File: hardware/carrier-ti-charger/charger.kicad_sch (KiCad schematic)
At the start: 42 parts, among them J2 NTC, Q10 2N7002, Q12 2N7002, Q13 CSD17575Q3, SW4 RESET 6x6, U14 TPS259474LRPWR, U4 BQ25798RQMR

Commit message: Refine resistors.
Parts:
- L1: value 2.2uH FXL0630-2R2-M -> 2.2uH FC-ALX4030D-2R2MT; footprint carrier:IND-SMD_L7.0-W6.6_FXL0630 -> carrier:IND-SMD_L4.2-W4.2_FC-ALX4030D; LCSC C167218 -> C5370906
- R77: footprint carrier:R_0805_2012Metric_NoSilk -> Resistor_SMD:R_0603_1608Metric; LCSC C706247 -> C2924137; MPN RT0805BRD075K36L -> AR03BTCX5361A; Manufacturer YAGEO -> Viking Tech
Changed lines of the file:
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@@
 			)
 		)
-		(property "Value" "2.2uH FXL0630-2R2-M"
+		(property "Value" "2.2uH FC-ALX4030D-2R2MT"
 			(at 139.7 69.85 0)
 			(show_name no)
@@
 			)
 		)
-		(property "Footprint" "carrier:IND-SMD_L7.0-W6.6_FXL0630"
+		(property "Footprint" "carrier:IND-SMD_L4.2-W4.2_FC-ALX4030D"
 			(at 139.7 64.77 0)
 			(hide yes)
@@
 			)
 		)
-		(property "Datasheet" "https://datasheet.lcsc.com/datasheet/pdf/7ccab6d15d9e909aa3f3d55ed931dfcf.pdf?productCode=C167216"
+		(property "Datasheet" "https://datasheet.lcsc.com/datasheet/pdf/4f0a80287f31a1fb9e399a39619e691e.pdf?productCode=C5370906"
 			(at 139.7 64.77 0)
 			(hide yes)
@@
 			)
 		)
-		(property "LCSC" "C167218"
+		(property "LCSC" "C5370906"
 			(at 139.7 64.77 0)
 			(hide yes)
@@
 			)
 		)
-		(property "Footprint" "carrier:R_0805_2012Metric_NoSilk"
+		(property "Footprint" "Resistor_SMD:R_0603_1608Metric"
 			(at 215.9 57.15 0)
 			(hide yes)
@@
 			)
 		)
-		(property "Datasheet" "https://datasheet.lcsc.com/datasheet/pdf/46d7760c582640714d605308a25a220a.pdf?productCode=C706247"
+		(property "Datasheet" "https://datasheet.lcsc.com/datasheet/pdf/5bf30c62a4b85499d309118a7d825f44.pdf?productCode=C2924137"
 			(at 215.9 57.15 0)
 			(hide yes)
@@
 			)
 		)
-		(property "Description" "OVLO divider, 0.1%, 25 ppm/C, 125 mW, 150 V"
+		(property "Description" "OVLO divider, 0.1%, 25 ppm/C, 100 mW, 75 V"
 			(at 215.9 57.15 0)
 			(hide yes)
@@
 			)
 		)
-		(property "LCSC" "C706247"
+		(property "LCSC" "C2924137"
 			(at 215.9 57.15 0)
 			(hide yes)
@@
 			)
 		)
-		(property "MPN" "RT0805BRD075K36L"
+		(property "MPN" "AR03BTCX5361A"
 			(at 215.9 57.15 0)
 			(hide yes)
@@
 			)
 		)
-		(property "Manufacturer" "YAGEO"
+		(property "Manufacturer" "Viking Tech"
 			(at 215.9 57.15 0)
 			(hide yes)

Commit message: Fix missing parts.
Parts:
- D10: value BAT54WS -> 1N4148WS; LCSC C22629 -> C2128; MPN (none) -> 1N4148WS
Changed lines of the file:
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@@
 			)
 		)
-		(property "Value" "BAT54WS"
+		(property "Value" "1N4148WS"
 			(at 38.1 92.71 0)
 			(show_name no)
@@
 			)
 		)
-		(property "LCSC" "C22629"
+		(property "LCSC" "C2128"
 			(at 38.1 90.17 0)
 			(hide yes)
+			(show_name no)
+			(do_not_autoplace no)
+			(effects
+				(font
+					(size 1.27 1.27)
+				)
+			)
+		)
+		(property "MPN" "1N4148WS"
+			(at 38.1 90.17 0)
+			(hide yes)

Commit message: Consolidate bom.
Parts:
- C33: value 22u 16V X7R -> 22u 10V X7R; footprint Capacitor_SMD:C_1206_3216Metric -> Capacitor_SMD:C_0805_2012Metric; LCSC C385906 -> C907991
- C43, C44, C46, C5, C50: value 100n 50V -> 100n 16V; footprint Capacitor_SMD:C_0603_1608Metric -> carrier:C_0402_1005Metric_NoSilk; LCSC C14663 -> C1525; MPN (none) -> CL05B104KO5NNNC
- R56: footprint Resistor_SMD:R_0603_1608Metric -> carrier:R_0402_1005Metric_NoSilk; LCSC C23162 -> C25900; MPN (none) -> 0402WGF4701TCE
- R60: footprint Resistor_SMD:R_0603_1608Metric -> carrier:R_0402_1005Metric_NoSilk; LCSC C2933258 -> C49196905; MPN (none) -> FRC0402F7683TS
- R77: value 5.36k -> 4.7k 1%; footprint Resistor_SMD:R_0603_1608Metric -> carrier:R_0402_1005Metric_NoSilk; LCSC C2924137 -> C25900; MPN AR03BTCX5361A -> 0402WGF4701TCE; TCR 25 ppm/C -> 100 ppm/C; Tolerance 0.1% -> 1%
- R78: value 1.5k -> 1.24k 0.1%; LCSC C281775 -> C2984409; MPN RT0402BRD071K5L -> ARG02BTC1241
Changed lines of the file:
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@@
 			)
 		)
-		(property "Value" "100n 50V"
+		(property "Value" "100n 16V"
 			(at 182.88 52.07 0)
 			(show_name no)
@@
 			)
 		)
-		(property "Footprint" "Capacitor_SMD:C_0603_1608Metric"
+		(property "Footprint" "carrier:C_0402_1005Metric_NoSilk"
 			(at 180.34 50.8 0)
 			(hide yes)
@@
 			)
 		)
-		(property "LCSC" "C14663"
+		(property "LCSC" "C1525"
+			(at 180.34 50.8 0)
+			(hide yes)
+			(show_name no)
+			(do_not_autoplace no)
+			(effects
+				(font
+					(size 1.27 1.27)
+				)
+			)
+		)
+		(property "MPN" "CL05B104KO5NNNC"
 			(at 180.34 50.8 0)
 			(hide yes)
@@
 			)
 		)
-		(property "Value" "100n 50V"
+		(property "Value" "100n 16V"
 			(at 194.31 140.97 0)
 			(show_name no)
@@
 			)
 		)
-		(property "Footprint" "Capacitor_SMD:C_0603_1608Metric"
+		(property "Footprint" "carrier:C_0402_1005Metric_NoSilk"
 			(at 191.77 139.7 0)
 			(hide yes)
@@
 			)
 		)
-		(property "LCSC" "C14663"
+		(property "LCSC" "C1525"
+			(at 191.77 139.7 0)
+			(hide yes)
+			(show_name no)
+			(do_not_autoplace no)
+			(effects
+				(font
+					(size 1.27 1.27)
+				)
+			)
+		)
+		(property "MPN" "CL05B104KO5NNNC"
 			(at 191.77 139.7 0)
 			(hide yes)
@@
 			)
 		)
-		(property "Value" "100n 50V"
+		(property "Value" "100n 16V"
 			(at 31.75 59.69 0)
 			(show_name no)
@@
 			)
 		)
-		(property "Footprint" "Capacitor_SMD:C_0603_1608Metric"
+		(property "Footprint" "carrier:C_0402_1005Metric_NoSilk"
 			(at 29.21 58.42 0)
 			(hide yes)
@@
 			)
 		)
-		(property "LCSC" "C14663"
+		(property "LCSC" "C1525"
+			(at 29.21 58.42 0)
+			(hide yes)
+			(show_name no)
+			(do_not_autoplace no)
+			(effects
+				(font
+					(size 1.27 1.27)
+				)
+			)
+		)
+		(property "MPN" "CL05B104KO5NNNC"
 			(at 29.21 58.42 0)
 			(hide yes)
@@
 			)
 		)
-		(property "Value" "1.5k"
+		(property "Value" "1.24k 0.1%"
 			(at 218.44 66.04 0)
 			(show_name no)
@@
 			)
 		)
-		(property "Description" "OVLO divider, 0.1%, 25 ppm/C, 62.5 mW, 50 V"
+		(property "Description" "OVLO divider bottom, U14 USB side, 0.1%, 25 ppm/C"
 			(at 215.9 64.77 0)
 			(hide yes)
@@
 			)
 		)
-		(property "LCSC" "C281775"
+		(property "LCSC" "C2984409"
 			(at 215.9 64.77 0)
 			(hide yes)
@@
 			)
 		)
-		(property "MPN" "RT0402BRD071K5L"
+		(property "MPN" "ARG02BTC1241"
 			(at 215.9 64.77 0)
 			(hide yes)
@@
 			)
 		)
-		(property "Value" "100n 50V"
+		(property "Value" "100n 16V"
 			(at 77.47 59.69 0)
 			(show_name no)
@@
 			)
 		)
-		(property "Footprint" "Capacitor_SMD:C_0603_1608Metric"
+		(property "Footprint" "carrier:C_0402_1005Metric_NoSilk"
 			(at 74.93 58.42 0)
 			(hide yes)
@@
 			)
 		)
-		(property "LCSC" "C14663"
+		(property "LCSC" "C1525"
+			(at 74.93 58.42 0)
+			(hide yes)
+			(show_name no)
+			(do_not_autoplace no)
+			(effects
+				(font
+					(size 1.27 1.27)
+				)
+			)
+		)
+		(property "MPN" "CL05B104KO5NNNC"
 			(at 74.93 58.42 0)
 			(hide yes)
@@
 			)
 		)
-		(property "Value" "100n 50V"
+		(property "Value" "100n 16V"
 			(at 215.9 91.44 0)
 			(show_name no)
@@
 			)
 		)
-		(property "Footprint" "Capacitor_SMD:C_0603_1608Metric"
+		(property "Footprint" "carrier:C_0402_1005Metric_NoSilk"
 			(at 218.44 90.17 0)
 			(hide yes)
@@
 			)
 		)
-		(property "LCSC" "C14663"
+		(property "LCSC" "C1525"
+			(at 218.44 90.17 0)
+			(hide yes)
+			(show_name no)
+			(do_not_autoplace no)
+			(effects
+				(font
+					(size 1.27 1.27)
+				)
+			)
+		)
+		(property "MPN" "CL05B104KO5NNNC"
 			(at 218.44 90.17 0)
 			(hide yes)
@@
 			)
 		)
-		(property "Value" "22u 16V X7R"
+		(property "Value" "22u 10V X7R"
 			(at 167.64 52.07 0)
 			(show_name no)
@@
 			)
 		)
-		(property "Footprint" "Capacitor_SMD:C_1206_3216Metric"
+		(property "Footprint" "Capacitor_SMD:C_0805_2012Metric"
 			(at 165.1 50.8 0)
 			(hide yes)
@@
 			)
 		)
-		(property "LCSC" "C385906"
+		(property "LCSC" "C907991"
 			(at 165.1 50.8 0)
 			(hide yes)
@@
 			)
 		)
-		(property "Value" "5.36k"
+		(property "Value" "4.7k 1%"
 			(at 218.44 58.42 0)
 			(show_name no)
@@
 			)
 		)
-		(property "Footprint" "Resistor_SMD:R_0603_1608Metric"
+		(property "Footprint" "carrier:R_0402_1005Metric_NoSilk"
 			(at 215.9 57.15 0)
 			(hide yes)
@@
 			)
 		)
-		(property "Description" "OVLO divider, 0.1%, 25 ppm/C, 100 mW, 75 V"
+		(property "Description" "OVLO divider top, U14 USB side"
 			(at 215.9 57.15 0)
 			(hide yes)
@@
 			)
 		)
-		(property "LCSC" "C2924137"
+		(property "LCSC" "C25900"
 			(at 215.9 57.15 0)
 			(hide yes)
@@
 			)
 		)
-		(property "MPN" "AR03BTCX5361A"
+		(property "MPN" "0402WGF4701TCE"
 			(at 215.9 57.15 0)
 			(hide yes)
@@
 			)
 		)
-		(property "Tolerance" "0.1%"
+		(property "Tolerance" "1%"
 			(at 215.9 57.15 0)
 			(hide yes)
@@
 			)
 		)
-		(property "TCR" "25 ppm/C"
+		(property "TCR" "100 ppm/C"
 			(at 215.9 57.15 0)
 			(hide yes)
@@
 			)
 		)
-		(property "Footprint" "Resistor_SMD:R_0603_1608Metric"
+		(property "Footprint" "carrier:R_0402_1005Metric_NoSilk"
 			(at 54.61 109.22 0)
 			(hide yes)
@@
 			)
 		)
-		(property "LCSC" "C23162"
+		(property "LCSC" "C25900"
+			(at 54.61 109.22 0)
+			(hide yes)
+			(show_name no)
+			(do_not_autoplace no)
+			(effects
+				(font
+					(size 1.27 1.27)
+				)
+			)
+		)
+		(property "MPN" "0402WGF4701TCE"
 			(at 54.61 109.22 0)
 			(hide yes)
@@
 			)
 		)
-		(property "Footprint" "Resistor_SMD:R_0603_1608Metric"
+		(property "Footprint" "carrier:R_0402_1005Metric_NoSilk"
 			(at 92.71 114.3 0)
 			(hide yes)
@@
 			)
 		)
-		(property "Datasheet" ""
+		(property "Datasheet" "https://www.lcsc.com/product-detail/C49196905.html"
 			(at 92.71 114.3 0)
 			(hide yes)
@@
 			)
 		)
-		(property "LCSC" "C2933258"
+		(property "LCSC" "C49196905"
+			(at 92.71 114.3 0)
+			(hide yes)
+			(show_name no)
+			(do_not_autoplace no)
+			(effects
+				(font
+					(size 1.27 1.27)
+				)
+			)
+		)
+		(property "MPN" "FRC0402F7683TS"
 			(at 92.71 114.3 0)
 			(hide yes)

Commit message: Polishing.
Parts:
- renumbered J2 to J12
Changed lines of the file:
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@@
 		(in_pos_files yes)
 		(dnp yes)
-		(property "Reference" "J2"
+		(property "Reference" "J12"
 			(at 44.45 137.16 0)
 			(show_name no)
@@
 			(project "carrier"
 				(path "/1d76d2ec-7795-4c71-8167-b1182c3ebc1d/ca5da11d-56a4-4cac-94d5-ee3030474f4d"
-					(reference "J2")
+					(reference "J12")
 					(unit 1)
 				)

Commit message: Polishing.
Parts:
- R59: value 80.6k 1% -> 82k 1%; LCSC C23249 -> C23254; MPN (none) -> 0603WAF8202T5E; Manufacturer (none) -> UNI-ROYAL; TCR (none) -> 100 ppm/°C; Tolerance (none) -> 1%
- R72: value 1.65k -> 1.8k; LCSC C22845 -> C4177; MPN 0603WAF1651T5E -> 0603WAF1801T5E; Manufacturer (none) -> UNI-ROYAL; TCR (none) -> 100 ppm/°C; Tolerance (none) -> 1%
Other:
- note added: "D+/D- BC1.2 on chip, CC on U15 FUSB303B (USB input sheet). Ship FET Q13, QON reset SW4. PROG 4.7k = 1S, 750 kHz. ILIM_HIZ 2.2 V = 1.5 A clamp, firmware lifts it (EN_EXTILIM) on a 3 A advertisement. TS 82k/768k: 2.7/42.6 C."
- note removed: "D+/D- BC1.2 on chip, CC on U15 FUSB303B (USB input sheet). Ship FET Q13, QON reset SW4. PROG 4.7k = 1S, 750 kHz. ILIM_HIZ 2.2 V = 1.5 A clamp, firmware lifts it (EN_EXTILIM) on a 3 A advertisement. TS 80.6k/768k: 3/43 C."
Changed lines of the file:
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@@
 		)
 	)
-	(text "D+/D- BC1.2 on chip, CC on U15 FUSB303B (USB input sheet). Ship FET Q13, QON reset SW4. PROG 4.7k = 1S, 750 kHz. ILIM_HIZ 2.2 V = 1.5 A clamp, firmware lifts it (EN_EXTILIM) on a 3 A advertisement. TS 80.6k/768k: 3/43 C."
+	(text "D+/D- BC1.2 on chip, CC on U15 FUSB303B (USB input sheet). Ship FET Q13, QON reset SW4. PROG 4.7k = 1S, 750 kHz. ILIM_HIZ 2.2 V = 1.5 A clamp, firmware lifts it (EN_EXTILIM) on a 3 A advertisement. TS 82k/768k: 2.7/42.6 C."
 		(exclude_from_sim no)
 		(at 20.32 30.48 0)
@@
 			)
 		)
-		(property "Value" "1.65k"
+		(property "Value" "1.8k"
 			(at 246.38 144.78 0)
 			(show_name no)
@@
 			)
 		)
-		(property "Datasheet" ""
+		(property "Datasheet" "https://www.uni-royal.cn/en/images/userfile/file/1753752986c56505e6d9ab55c7.pdf"
 			(at 243.84 143.51 0)
 			(hide yes)
@@
 			)
 		)
-		(property "LCSC" "C22845"
+		(property "LCSC" "C4177"
+			(at 243.84 143.51 0)
+			(hide yes)
+			(show_name no)
+			(do_not_autoplace no)
+			(effects
+				(font
+					(size 1.27 1.27)
+				)
+			)
+		)
+		(property "TCR" "100 ppm/°C"
+			(at 243.84 143.51 0)
+			(hide yes)
+			(show_name no)
+			(do_not_autoplace no)
+			(effects
+				(font
+					(size 1.27 1.27)
+				)
+			)
+		)
+		(property "Tolerance" "1%"
+			(at 243.84 143.51 0)
+			(hide yes)
+			(show_name no)
+			(do_not_autoplace no)
+			(effects
+				(font
+					(size 1.27 1.27)
+				)
+			)
+		)
+		(property "Manufacturer" "UNI-ROYAL"
 			(at 243.84 143.51 0)
 			(hide yes)
@@
 			)
 		)
-		(property "MPN" "0603WAF1651T5E"
+		(property "MPN" "0603WAF1801T5E"
 			(at 243.84 143.51 0)
 			(hide yes)
@@
 			)
 		)
-		(property "Value" "80.6k 1%"
+		(property "Value" "82k 1%"
 			(at 74.93 115.57 0)
 			(show_name no)
@@
 			)
 		)
-		(property "Datasheet" ""
+		(property "Datasheet" "https://www.uni-royal.cn/en/images/userfile/file/1753752986c56505e6d9ab55c7.pdf"
 			(at 77.47 114.3 0)
 			(hide yes)
@@
 			)
 		)
-		(property "LCSC" "C23249"
+		(property "LCSC" "C23254"
+			(at 77.47 114.3 0)
+			(hide yes)
+			(show_name no)
+			(do_not_autoplace no)
+			(effects
+				(font
+					(size 1.27 1.27)
+				)
+			)
+		)
+		(property "TCR" "100 ppm/°C"
+			(at 77.47 114.3 0)
+			(hide yes)
+			(show_name no)
+			(do_not_autoplace no)
+			(effects
+				(font
+					(size 1.27 1.27)
+				)
+			)
+		)
+		(property "Tolerance" "1%"
+			(at 77.47 114.3 0)
+			(hide yes)
+			(show_name no)
+			(do_not_autoplace no)
+			(effects
+				(font
+					(size 1.27 1.27)
+				)
+			)
+		)
+		(property "Manufacturer" "UNI-ROYAL"
+			(at 77.47 114.3 0)
+			(hide yes)
+			(show_name no)
+			(do_not_autoplace no)
+			(effects
+				(font
+					(size 1.27 1.27)
+				)
+			)
+		)
+		(property "MPN" "0603WAF8202T5E"
 			(at 77.47 114.3 0)
 			(hide yes)

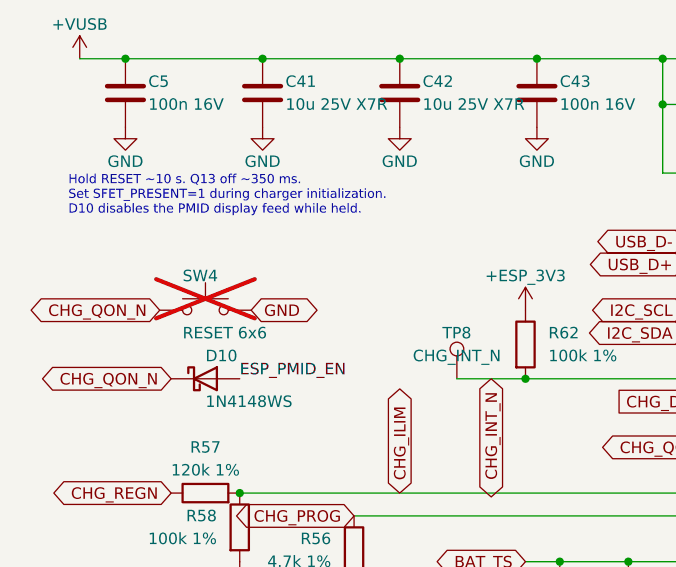
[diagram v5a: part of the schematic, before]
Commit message: Consolidate BOM, add GNSS listen to ESP.
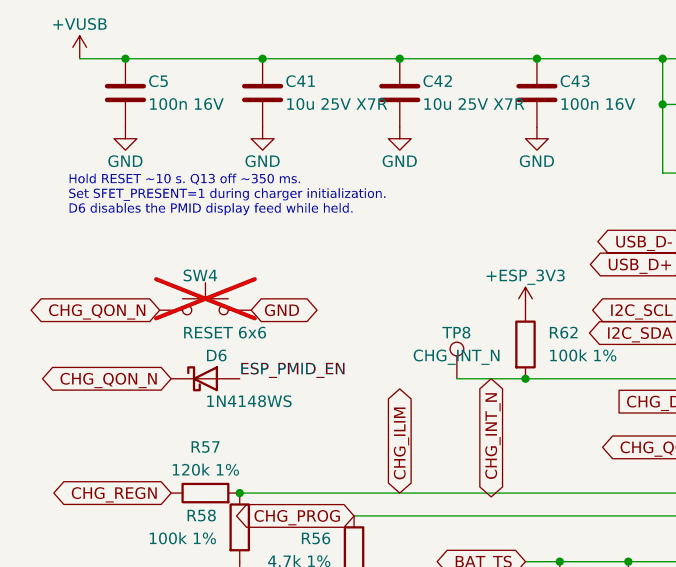
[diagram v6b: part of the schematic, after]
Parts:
- C43, C44, C46, C5, C50: footprint carrier:C_0402_1005Metric_NoSilk -> Mark:C_0402_1005Metric_NoSilk
- J12: footprint carrier:JST_PH_B2B-PH-K_1x02_P2.00mm_Vertical_R10 -> Mark:JST_PH_B2B-PH-K_1x02_P2.00mm_Vertical_R10
- L1: footprint carrier:IND-SMD_L4.2-W4.2_FC-ALX4030D -> Mark:IND-SMD_L4.2-W4.2_FC-ALX4030D; symbol carrier:CKST0603-2.2UH_M -> Mark:CKST0603-2.2UH_M
- Q13: footprint carrier:VSON-8_3.3x3.3mm_CSD17575Q3 -> Mark:VSON-8_3.3x3.3mm_CSD17575Q3
- R56, R60, R77, R78: footprint carrier:R_0402_1005Metric_NoSilk -> Mark:R_0402_1005Metric_NoSilk
- SW4: now left out of the parts list
- TP8: footprint carrier:TestPoint_Pad_D1.5mm -> Mark:TestPoint_Pad_D1.5mm
- U14: footprint carrier:VQFN-10_L2.0-W2.0-P0.45-HR_LM73100 -> Mark:VQFN-10_L2.0-W2.0-P0.45-HR_LM73100; symbol carrier:TPS259474LRPW -> Mark:TPS259474LRPW
- renumbered D10 to D6
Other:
- note added: "Hold RESET ~10 s. Q13 off ~350 ms. Set SFET_PRESENT=1 during charger initialization. D6 disables the PMID display feed while held."
- note removed: "Hold RESET ~10 s. Q13 off ~350 ms. Set SFET_PRESENT=1 during charger initialization. D10 disables the PMID display feed while held."
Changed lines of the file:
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@@
 		(rev "A")
 	)
-	(text "Hold RESET ~10 s. Q13 off ~350 ms.\nSet SFET_PRESENT=1 during charger initialization.\nD10 disables the PMID display feed while held."
+	(text "Hold RESET ~10 s. Q13 off ~350 ms.\nSet SFET_PRESENT=1 during charger initialization.\nD6 disables the PMID display feed while held."
 		(exclude_from_sim no)
 		(at 22.86 69.85 0)
@@
 	)
 	(symbol
-		(lib_id "carrier:+VSYS")
+		(lib_id "Mark:+VSYS")
 		(at 196.85 135.89 0)
 		(unit 1)
@@
 		(in_pos_files yes)
 		(dnp no)
-		(property "Reference" "D10"
+		(property "Reference" "D6"
 			(at 38.1 87.63 0)
 			(show_name no)
@@
 			(project "carrier"
 				(path "/1d76d2ec-7795-4c71-8167-b1182c3ebc1d/ca5da11d-56a4-4cac-94d5-ee3030474f4d"
-					(reference "D10")
+					(reference "D6")
 					(unit 1)
 				)
@@
 			)
 		)
-		(property "Footprint" "carrier:C_0402_1005Metric_NoSilk"
+		(property "Footprint" "Mark:C_0402_1005Metric_NoSilk"
 			(at 180.34 50.8 0)
 			(hide yes)
@@
 			)
 		)
-		(property "Footprint" "carrier:TestPoint_Pad_D1.5mm"
+		(property "Footprint" "Mark:TestPoint_Pad_D1.5mm"
 			(at 66.04 90.17 0)
 			(hide yes)
@@
 			)
 		)
-		(property "Footprint" "carrier:C_0402_1005Metric_NoSilk"
+		(property "Footprint" "Mark:C_0402_1005Metric_NoSilk"
 			(at 191.77 139.7 0)
 			(hide yes)
@@
 			)
 		)
-		(property "Footprint" "carrier:C_0402_1005Metric_NoSilk"
+		(property "Footprint" "Mark:C_0402_1005Metric_NoSilk"
 			(at 29.21 58.42 0)
 			(hide yes)
@@
 			)
 		)
-		(property "Footprint" "carrier:R_0402_1005Metric_NoSilk"
+		(property "Footprint" "Mark:R_0402_1005Metric_NoSilk"
 			(at 215.9 64.77 0)
 			(hide yes)
@@
 	)
 	(symbol
-		(lib_id "carrier:+ESP_3V3")
+		(lib_id "Mark:+ESP_3V3")
 		(at 73.66 82.55 0)
 		(unit 1)
@@
 			)
 		)
-		(property "Footprint" "carrier:C_0402_1005Metric_NoSilk"
+		(property "Footprint" "Mark:C_0402_1005Metric_NoSilk"
 			(at 74.93 58.42 0)
 			(hide yes)
@@
 			)
 		)
-		(property "Footprint" "carrier:VSON-8_3.3x3.3mm_CSD17575Q3"
+		(property "Footprint" "Mark:VSON-8_3.3x3.3mm_CSD17575Q3"
 			(at 167.64 115.57 0)
 			(hide yes)
@@
 	)
 	(symbol
-		(lib_id "carrier:CKST0603-2.2UH_M")
+		(lib_id "Mark:CKST0603-2.2UH_M")
 		(at 139.7 64.77 0)
 		(unit 1)
@@
 			)
 		)
-		(property "Footprint" "carrier:IND-SMD_L4.2-W4.2_FC-ALX4030D"
+		(property "Footprint" "Mark:IND-SMD_L4.2-W4.2_FC-ALX4030D"
 			(at 139.7 64.77 0)
 			(hide yes)
@@
 			)
 		)
-		(property "Footprint" "carrier:C_0402_1005Metric_NoSilk"
+		(property "Footprint" "Mark:C_0402_1005Metric_NoSilk"
 			(at 218.44 90.17 0)
 			(hide yes)
@@
 	)
 	(symbol
-		(lib_id "carrier:+VUSB")
+		(lib_id "Mark:+VUSB")
 		(at 59.69 138.43 0)
 		(unit 1)
@@
 			)
 		)
-		(property "Footprint" "carrier:JST_PH_B2B-PH-K_1x02_P2.00mm_Vertical_R10"
+		(property "Footprint" "Mark:JST_PH_B2B-PH-K_1x02_P2.00mm_Vertical_R10"
 			(at 41.91 138.43 0)
 			(hide yes)
@@
 			)
 		)
-		(property "Footprint" "carrier:R_0402_1005Metric_NoSilk"
+		(property "Footprint" "Mark:R_0402_1005Metric_NoSilk"
 			(at 215.9 57.15 0)
 			(hide yes)
@@
 	)
 	(symbol
-		(lib_id "carrier:TPS259474LRPW")
+		(lib_id "Mark:TPS259474LRPW")
 		(at 250.19 91.44 0)
 		(unit 1)
@@
 			)
 		)
-		(property "Footprint" "carrier:VQFN-10_L2.0-W2.0-P0.45-HR_LM73100"
+		(property "Footprint" "Mark:VQFN-10_L2.0-W2.0-P0.45-HR_LM73100"
 			(at 250.19 91.44 0)
 			(hide yes)
@@
 			)
 		)
-		(property "Footprint" "carrier:R_0402_1005Metric_NoSilk"
+		(property "Footprint" "Mark:R_0402_1005Metric_NoSilk"
 			(at 54.61 109.22 0)
 			(hide yes)
@@
 	)
 	(symbol
-		(lib_id "carrier:+VUSB")
+		(lib_id "Mark:+VUSB")
 		(at 24.13 54.61 0)
 		(unit 1)
@@
 		(body_style 1)
 		(exclude_from_sim no)
-		(in_bom yes)
+		(in_bom no)
 		(on_board yes)
-		(in_pos_files yes)
+		(in_pos_files no)
 		(dnp yes)
 		(property "Reference" "SW4"
@@
 			)
 		)
-		(property "Footprint" "carrier:R_0402_1005Metric_NoSilk"
+		(property "Footprint" "Mark:R_0402_1005Metric_NoSilk"
 			(at 92.71 114.3 0)
 			(hide yes)
